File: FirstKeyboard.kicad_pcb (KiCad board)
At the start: 2 copper layers, 114.3 x 38.1 mm, 33 parts, among them SW1 SW_Push, U1 ATmega32U4-AU, Y1 16MHz

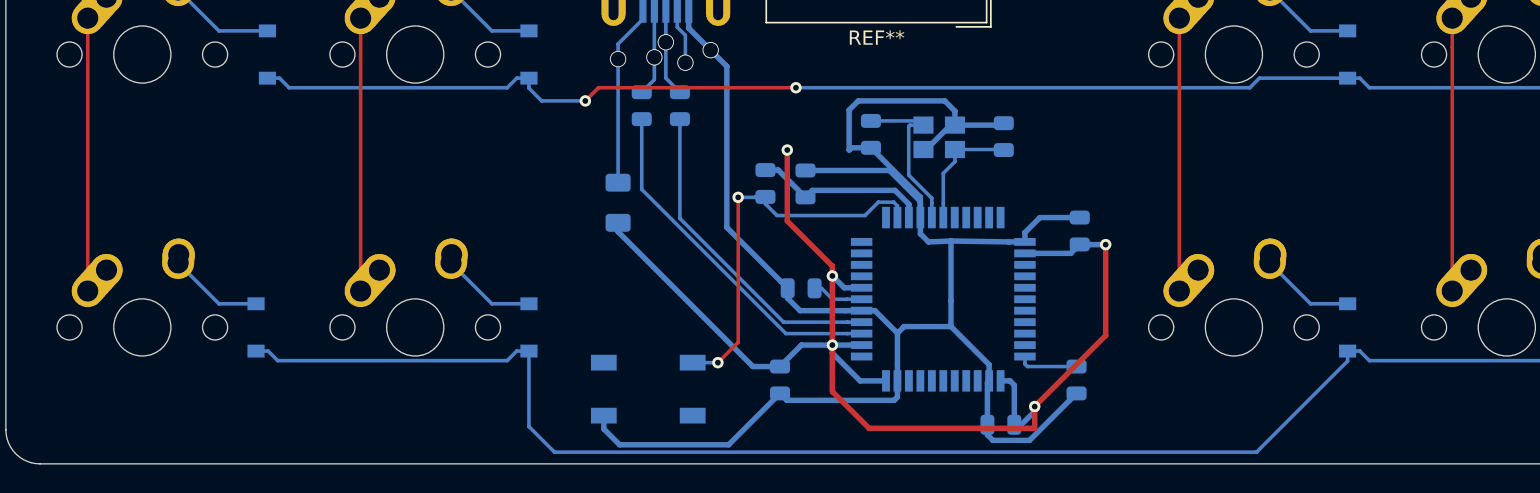
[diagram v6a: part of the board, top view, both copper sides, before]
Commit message: mapped r, c to pins and routed
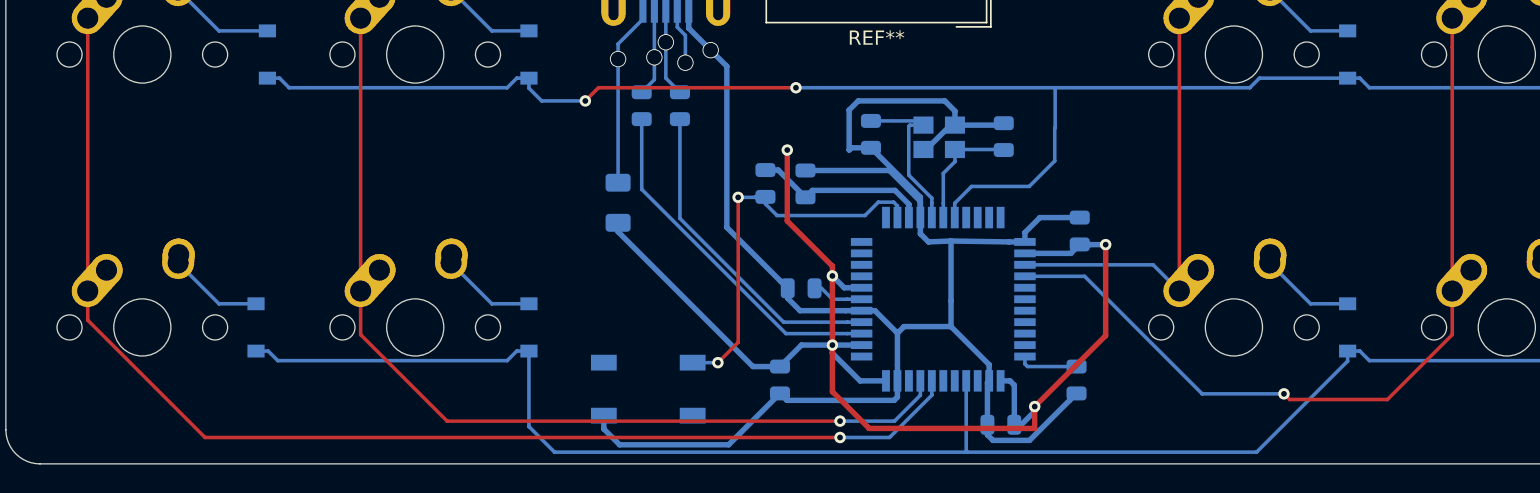
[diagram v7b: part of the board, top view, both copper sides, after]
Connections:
- U1 pad 18: Net-(U1-Pad18) -> Row0
- U1 pad 25: Net-(U1-Pad25) -> Col2
- U1 pad 26: Net-(U1-Pad26) -> Col3
- U1 pad 37: Net-(U1-Pad37) -> Row1
- U1 pad 40: Net-(U1-Pad40) -> Col0
- U1 pad 41: Net-(U1-Pad41) -> Col1
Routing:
- net Col0: track 19.0 -> 85.6 mm, vias 0 -> 1
- net Col1: track 19.0 -> 65.4 mm, vias 0 -> 1
- net Col3: track 19.0 -> 57.4 mm, vias 0 -> 1
- net Row0: track 97.3 -> 111.6 mm
- net Col2: track 19.0 -> 30.6 mm
- net Row1: track 105.7 -> 110.7 mm

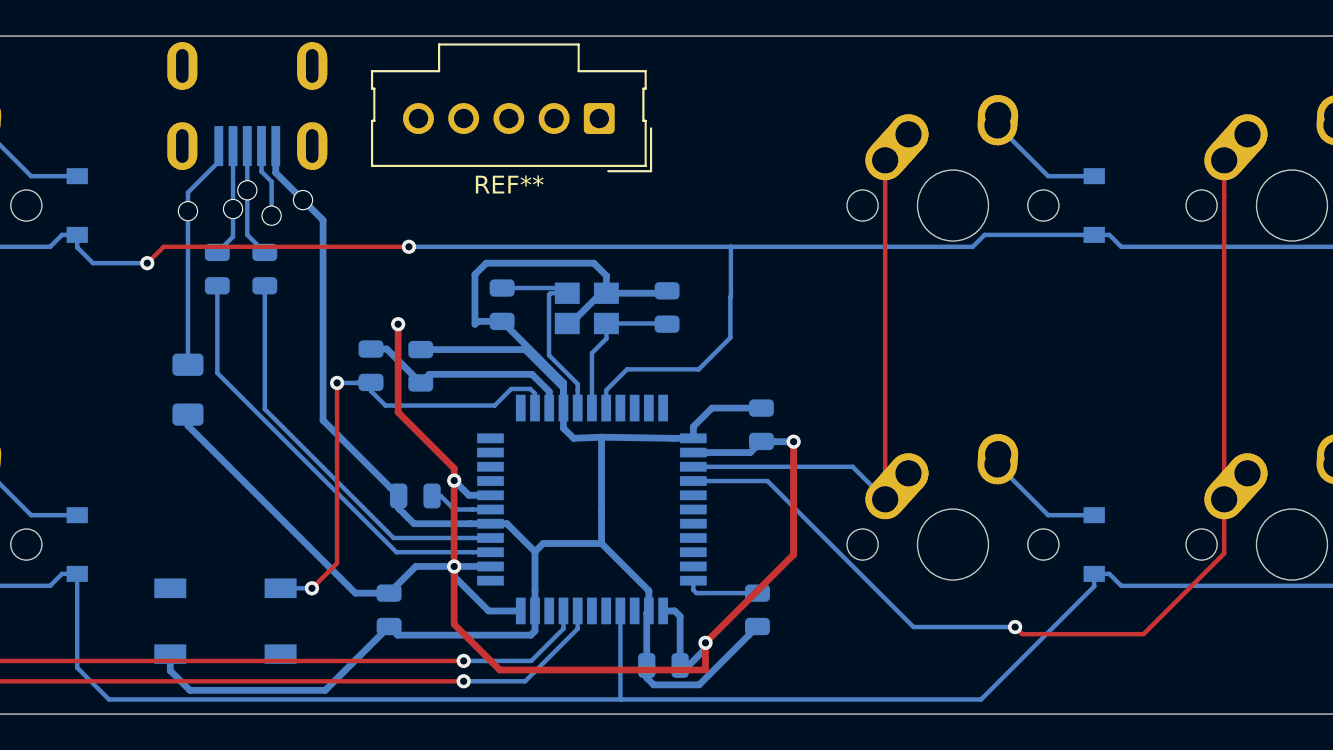
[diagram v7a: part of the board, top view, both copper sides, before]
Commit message: routed usb breakout
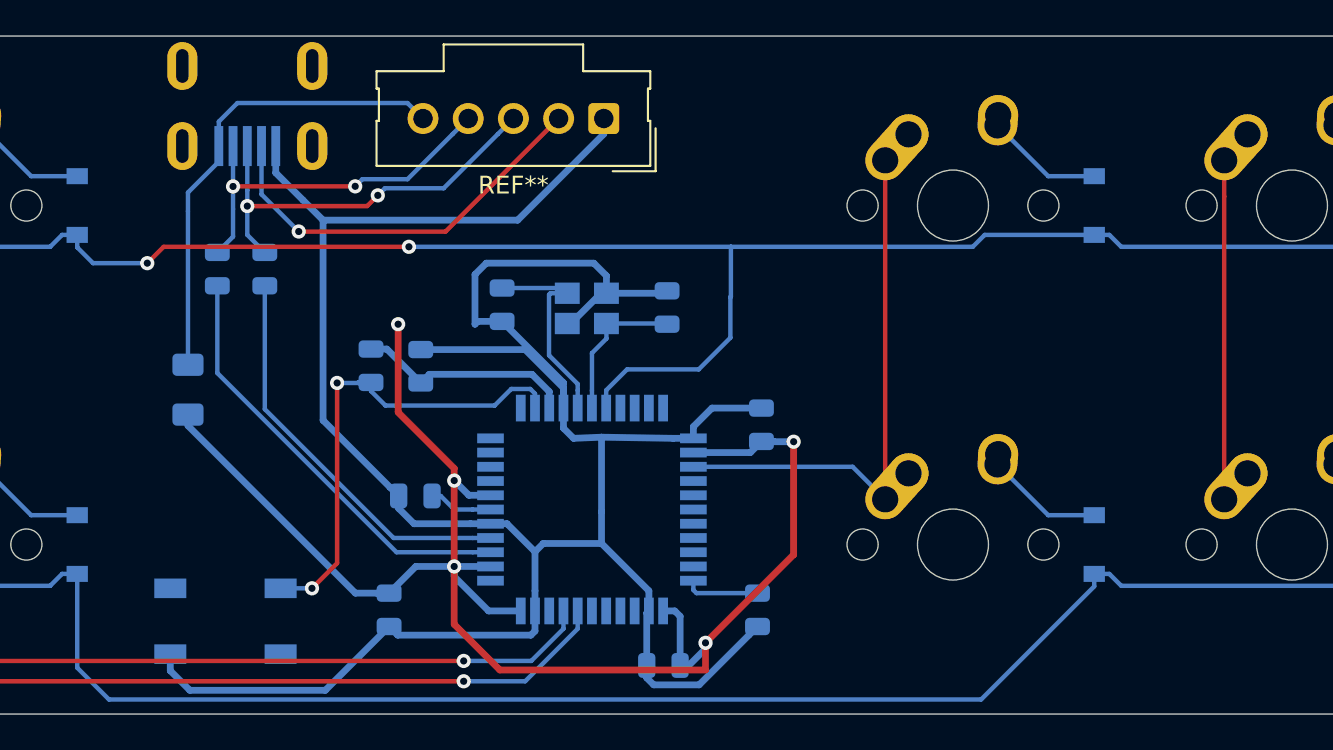
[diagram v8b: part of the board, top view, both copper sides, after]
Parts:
- moved REF** 0.25 mm to (162.9, 72.9)
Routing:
- net Col3: track 57.4 -> 19.0 mm, vias 1 -> 0
- net Net-(USB1-Pad2): track 4.15 -> 22.9 mm
- net GND: track 136.0 -> 154.6 mm, vias 1 -> 0
- net D+: track 6.38 -> 23.4 mm, vias 1 -> 2
- net D-: track 6.51 -> 21.3 mm, vias 1 -> 2
- net Net-(F1-Pad2): track 13.0 -> 26.6 mm, vias 1 -> 0
- net Row1: track 110.7 -> 105.7 mm
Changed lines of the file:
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@@
     (thickness 1.6)
     (drawings 8)
-    (tracks 267)
+    (tracks 277)
     (zones 0)
     (modules 33)
@@
   )
   (module Connector_Molex:Molex_SL_171971-0005_1x05_P2.54mm_Vertical (layer F.Cu)
-    (at 162.687 72.898 180)
+    (at 162.941 72.898 180)
     (descr "Molex Stackable Linear Connector, 171971-0005 (compatible alternatives: 171971-0105, 171971-0205), 5 Pins per row (https://www.molex.com/pdm_docs/sd/1719710002_sd.pdf), generated with kicad-footprint-generator")
     (tags "connector Molex SL vertical")
@@
   (segment (start 144.50675 74.44525) (end 144.50675 75.95125) (width 0.381) (layer B.Cu) (net 1))
   (segment (start 146.03775 77.48225) (end 147.164499 78.608999) (width 0.381) (layer B.Cu) (net 1))
-  (via (at 146.03775 77.48225) (size 1.143) (drill 1.016) (layers F.Cu B.Cu) (net 1))
+  (segment (start 162.941 73.768) (end 162.941 72.898) (width 0.381) (layer B.Cu) (net 1))
+  (segment (start 158.100001 78.608999) (end 162.941 73.768) (width 0.381) (layer B.Cu) (net 1))
+  (segment (start 147.164499 78.608999) (end 158.100001 78.608999) (width 0.381) (layer B.Cu) (net 1))
   (segment (start 158.904625 87.271473) (end 159.87425 88.241098) (width 0.381) (layer B.Cu) (net 2))
   (segment (start 159.87425 88.241098) (end 159.87425 89.169) (width 0.381) (layer B.Cu) (net 2))
@@
   (segment (start 131.831099 99.156401) (end 115.818901 99.156401) (width 0.25) (layer B.Cu) (net 9))
   (segment (start 133.35 98.4875) (end 132.5 98.4875) (width 0.25) (layer B.Cu) (net 9))
-  (segment (start 163.87425 105.46927) (end 163.87425 100.569) (width 0.25) (layer B.Cu) (net 9))
-  (segment (start 163.94949 105.54451) (end 163.87425 105.46927) (width 0.25) (layer B.Cu) (net 9))
-  (segment (start 163.94949 105.54451) (end 184.14299 105.54451) (width 0.25) (layer B.Cu) (net 9))
-  (segment (start 135.13551 105.54451) (end 163.94949 105.54451) (width 0.25) (layer B.Cu) (net 9))
+  (segment (start 135.13551 105.54451) (end 184.14299 105.54451) (width 0.25) (layer B.Cu) (net 9))
   (segment (start 130.7625 76.1375) (end 133.35 76.1375) (width 0.25) (layer B.Cu) (net 10))
   (segment (start 127.9125 73.2875) (end 130.7625 76.1375) (width 0.25) (layer B.Cu) (net 10))
@@
   (segment (start 139.573 77.054) (end 141.30675 75.32025) (width 0.25) (layer B.Cu) (net 16))
   (segment (start 139.573 78.105) (end 139.573 77.054) (width 0.25) (layer B.Cu) (net 16))
-  (via (at 139.573 78.105) (size 1.143) (drill 1.016) (layers F.Cu B.Cu) (net 16))
+  (segment (start 141.30675 73.07025) (end 141.30675 74.44525) (width 0.25) (layer B.Cu) (net 16))
+  (segment (start 142.348999 72.028001) (end 141.30675 73.07025) (width 0.25) (layer B.Cu) (net 16))
+  (segment (start 151.911001 72.028001) (end 142.348999 72.028001) (width 0.25) (layer B.Cu) (net 16))
+  (segment (start 152.781 72.898) (end 151.911001 72.028001) (width 0.25) (layer B.Cu) (net 16))
   (segment (start 102.5525 75.2475) (end 102.5525 94.2975) (width 0.25) (layer F.Cu) (net 17))
   (segment (start 158.52225 104.521) (end 155.067 104.521) (width 0.25) (layer B.Cu) (net 17))
@@
   (segment (start 197.8025 77.2795) (end 197.8025 94.2975) (width 0.25) (layer F.Cu) (net 20))
   (segment (start 197.8025 75.2475) (end 197.8025 77.2795) (width 0.25) (layer F.Cu) (net 20))
-  (via (at 186.055 101.473) (size 0.8) (drill 0.4) (layers F.Cu B.Cu) (net 20))
-  (segment (start 180.341998 101.473) (end 186.055 101.473) (width 0.25) (layer B.Cu) (net 20))
-  (segment (start 167.97425 93.269) (end 172.137998 93.269) (width 0.25) (layer B.Cu) (net 20))
-  (segment (start 172.137998 93.269) (end 180.341998 101.473) (width 0.25) (layer B.Cu) (net 20))
-  (segment (start 197.8025 97.343502) (end 197.8025 94.2975) (width 0.25) (layer F.Cu) (net 20))
-  (segment (start 186.454999 101.872999) (end 193.273003 101.872999) (width 0.25) (layer F.Cu) (net 20))
-  (segment (start 193.273003 101.872999) (end 197.8025 97.343502) (width 0.25) (layer F.Cu) (net 20))
-  (segment (start 186.055 101.473) (end 186.454999 101.872999) (width 0.25) (layer F.Cu) (net 20))
   (segment (start 142.90675 79.43675) (end 143.891 80.421) (width 0.25) (layer B.Cu) (net 21))
   (segment (start 142.90675 74.44525) (end 142.90675 76.93025) (width 0.25) (layer B.Cu) (net 21))
-  (segment (start 142.90675 76.93025) (end 142.90675 79.43675) (width 0.25) (layer B.Cu) (net 21))
-  (via (at 142.90675 76.93025) (size 1.143) (drill 1.016) (layers F.Cu B.Cu) (net 21))
+  (segment (start 142.90675 76.93025) (end 142.90675 77.81925) (width 0.25) (layer B.Cu) (net 21))
+  (segment (start 142.90675 77.81925) (end 142.90675 79.43675) (width 0.25) (layer B.Cu) (net 21))
+  (via (at 142.90675 77.81925) (size 0.8) (drill 0.4) (layers F.Cu B.Cu) (net 21))
+  (via (at 150.241 77.216) (size 0.8) (drill 0.4) (layers F.Cu B.Cu) (net 21))
+  (segment (start 142.90675 77.81925) (end 149.63775 77.81925) (width 0.25) (layer F.Cu) (net 21))
+  (segment (start 149.63775 77.81925) (end 150.241 77.216) (width 0.25) (layer F.Cu) (net 21))
+  (segment (start 156.991001 73.767999) (end 157.861 72.898) (width 0.25) (layer B.Cu) (net 21))
+  (segment (start 150.640999 76.816001) (end 153.942999 76.816001) (width 0.25) (layer B.Cu) (net 21))
+  (segment (start 153.942999 76.816001) (end 156.991001 73.767999) (width 0.25) (layer B.Cu) (net 21))
+  (segment (start 150.241 77.216) (end 150.640999 76.816001) (width 0.25) (layer B.Cu) (net 21))
   (segment (start 155.57425 96.469) (end 156.57425 96.469) (width 0.25) (layer B.Cu) (net 22))
   (segment (start 151.12865 96.469) (end 155.57425 96.469) (width 0.25) (layer B.Cu) (net 22))
@@
   (segment (start 141.34475 80.30025) (end 141.224 80.421) (width 0.25) (layer B.Cu) (net 23))
   (segment (start 142.10675 79.53825) (end 141.224 80.421) (width 0.25) (layer B.Cu) (net 23))
-  (segment (start 142.10675 74.44525) (end 142.10675 77.98425) (width 0.25) (layer B.Cu) (net 23))
+  (segment (start 142.10675 74.44525) (end 142.10675 76.71425) (width 0.25) (layer B.Cu) (net 23))
   (segment (start 142.10675 77.98425) (end 142.10675 79.53825) (width 0.25) (layer B.Cu) (net 23))
-  (via (at 142.10675 77.98425) (size 1.143) (drill 1.016) (layers F.Cu B.Cu) (net 23))
+  (segment (start 142.10675 76.71425) (end 142.10675 77.98425) (width 0.25) (layer B.Cu) (net 23))
+  (via (at 142.10675 76.71425) (size 0.8) (drill 0.4) (layers F.Cu B.Cu) (net 23))
+  (segment (start 142.10675 76.71425) (end 148.96475 76.71425) (width 0.25) (layer F.Cu) (net 23))
+  (via (at 148.971 76.708) (size 0.8) (drill 0.4) (layers F.Cu B.Cu) (net 23))
+  (segment (start 148.96475 76.71425) (end 148.971 76.708) (width 0.25) (layer F.Cu) (net 23))
+  (segment (start 154.451001 73.767999) (end 155.321 72.898) (width 0.25) (layer B.Cu) (net 23))
+  (segment (start 151.910999 76.308001) (end 154.451001 73.767999) (width 0.25) (layer B.Cu) (net 23))
+  (segment (start 149.370999 76.308001) (end 151.910999 76.308001) (width 0.25) (layer B.Cu) (net 23))
+  (segment (start 148.971 76.708) (end 149.370999 76.308001) (width 0.25) (layer B.Cu) (net 23))
   (segment (start 151.29224 97.269) (end 155.57425 97.269) (width 0.25) (layer B.Cu) (net 24))
   (segment (start 141.224 87.20076) (end 151.29224 97.269) (width 0.25) (layer B.Cu) (net 24))
@@
   (segment (start 168.14825 99.568) (end 167.97425 99.394) (width 0.25) (layer B.Cu) (net 26))
   (segment (start 171.577 99.568) (end 168.14825 99.568) (width 0.25) (layer B.Cu) (net 26))
-  (segment (start 143.70675 75.880291) (end 144.272 76.445541) (width 0.25) (layer B.Cu) (net 48))
-  (segment (start 143.70675 74.44525) (end 143.70675 75.880291) (width 0.25) (layer B.Cu) (net 48))
-  (segment (start 144.272 76.445541) (end 144.272 78.359) (width 0.25) (layer B.Cu) (net 48))
-  (segment (start 144.272 78.359) (end 144.272 78.359) (width 0.25) (layer B.Cu) (net 48))
-  (via (at 144.272 78.359) (size 1.143) (drill 1.016) (layers F.Cu B.Cu) (net 48))
+  (via (at 145.796 79.248) (size 0.8) (drill 0.4) (layers F.Cu B.Cu) (net 48))
+  (segment (start 143.70675 74.44525) (end 143.70675 77.15875) (width 0.25) (layer B.Cu) (net 48))
+  (segment (start 143.70675 77.15875) (end 145.796 79.248) (width 0.25) (layer B.Cu) (net 48))
+  (segment (start 154.051 79.248) (end 160.401 72.898) (width 0.25) (layer F.Cu) (net 48))
+  (segment (start 145.796 79.248) (end 154.051 79.248) (width 0.25) (layer F.Cu) (net 48))
 )
